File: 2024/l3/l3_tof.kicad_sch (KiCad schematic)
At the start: 4 parts

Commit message: final 0.9
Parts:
- U5, U6, U7, U8: footprint (none) -> Connector_PinHeader_2.54mm:PinHeader_1x06_P2.54mm_Vertical

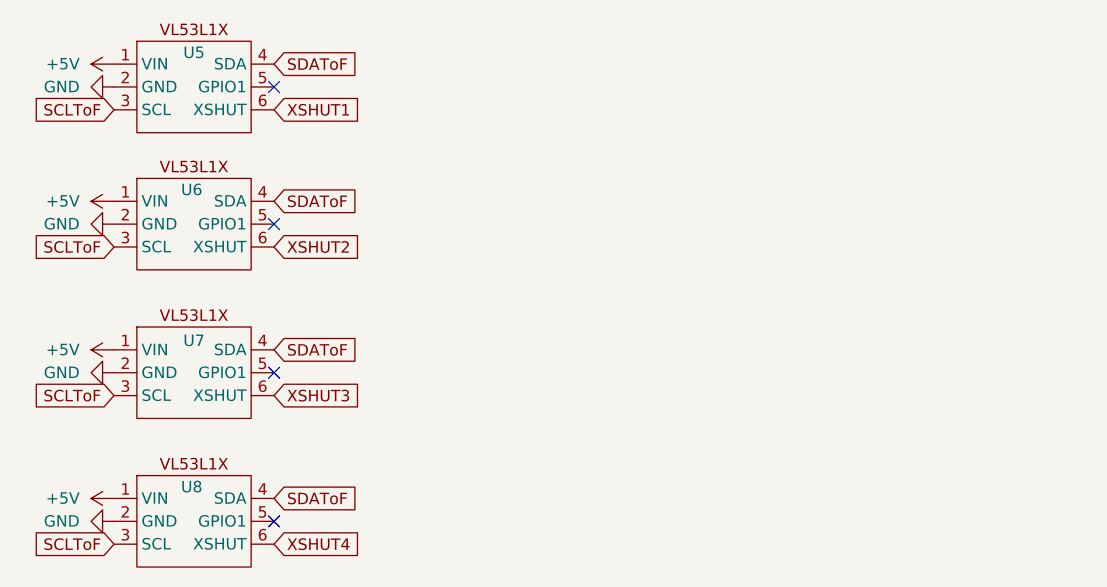
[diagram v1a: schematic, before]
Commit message: tf luna
gerber created for l1 and l2
l3 changed the tof from vl53l1x to tf luna
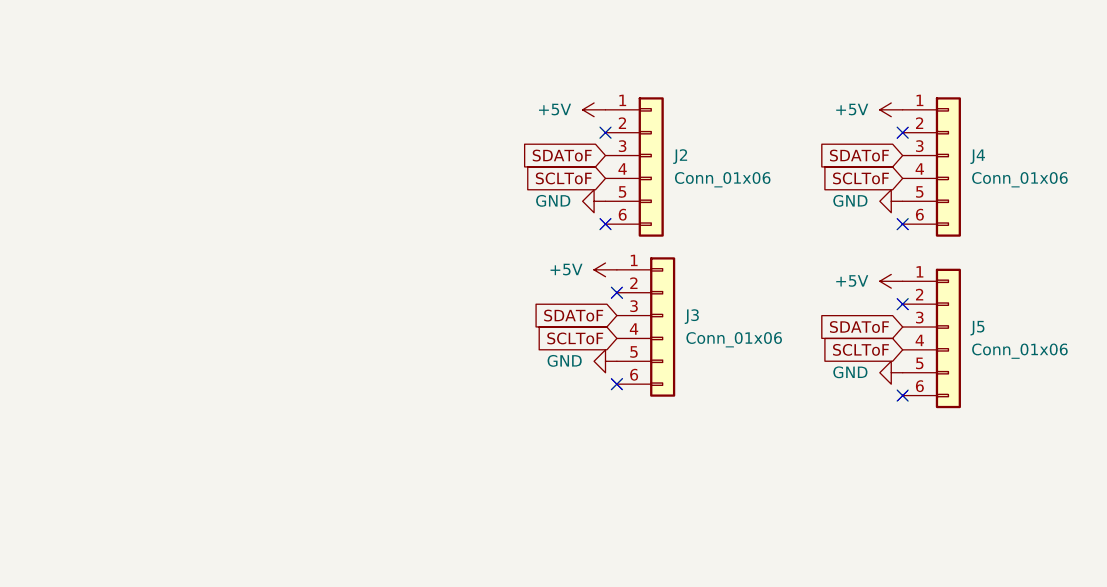
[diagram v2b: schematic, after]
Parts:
- removed U5, U6, U7, U8: ~, Connector_PinHeader_2.54mm:PinHeader_1x06_P2.54mm_Vertical, symbol Sensor_Distance:VL53L1X
- added J2, J3, J4, J5: Conn_01x06, Connector_PinHeader_2.54mm:PinHeader_1x06_P2.54mm_Vertical, symbol Connector_Generic:Conn_01x06
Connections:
- net +5V: now also J2.1 (Pin_1), J3.1 (Pin_1), J4.1 (Pin_1), J5.1 (Pin_1)
- net GND: now also J2.5 (Pin_5), J3.5 (Pin_5), J4.5 (Pin_5), J5.5 (Pin_5)
- net SCLToF: now also J2.4 (Pin_4), J3.4 (Pin_4), J4.4 (Pin_4), J5.4 (Pin_4)
- net SDAToF: now also J2.3 (Pin_3), J3.3 (Pin_3), J4.3 (Pin_3), J5.3 (Pin_3)
- no-connect marks 4 -> 8
